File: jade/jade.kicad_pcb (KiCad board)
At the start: 2 copper layers, 275.5 x 114.5 mm, 187 parts, among them J1 MJ-4PP-9, J2 OLED, J3 MJ-4PP-9, J4 OLED, SW1 SW_PUSH, SW10 SW_PUSH, SW11 SW_PUSH, SW12 SW_PUSH, SW13 SW_PUSH, SW14 SW_PUSH, SW15 SW_PUSH, SW16 SW_PUSH, SW17 SW_PUSH, SW18 SW_PUSH, SW19 SW_PUSH, SW2 SW_PUSH, SW20 SW_PUSH, SW21 SW_PUSH, SW22 SW_PUSH, SW23 SW_PUSH, SW24 SW_PUSH, SW25 SW_PUSH, SW26 SW_PUSH, SW27 SW_PUSH, SW28 SW_PUSH, SW29 SW_PUSH, SW3 SW_PUSH, SW30 SW_PUSH, SW31 SW_PUSH, SW32 SW_PUSH, SW33 SW_PUSH, SW34 SW_PUSH, SW35 SW_PUSH, SW36 SW_PUSH, SW37 SW_PUSH, SW38 SW_PUSH, SW39 SW_PUSH, SW4 SW_PUSH, SW40 SW_PUSH, SW41 SW_PUSH, SW42 SW_PUSH, SW43 SW_PUSH, SW44 SW_PUSH, SW45 SW_PUSH, SW46 SW_PUSH, SW47 SW_PUSH, SW48 SW_PUSH, SW5 SW_PUSH, SW6 SW_PUSH, SW7 SW_PUSH, SW8 SW_PUSH, SW9 SW_PUSH, U1 ProMicro, U2 ProMicro

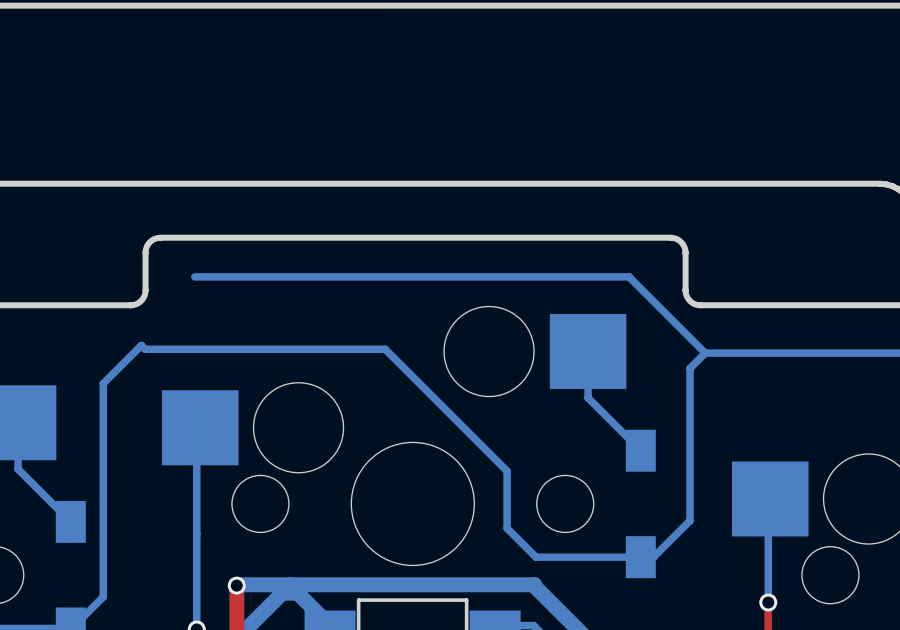
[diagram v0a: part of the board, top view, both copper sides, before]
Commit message: changed name again (cornetrack -> jade)
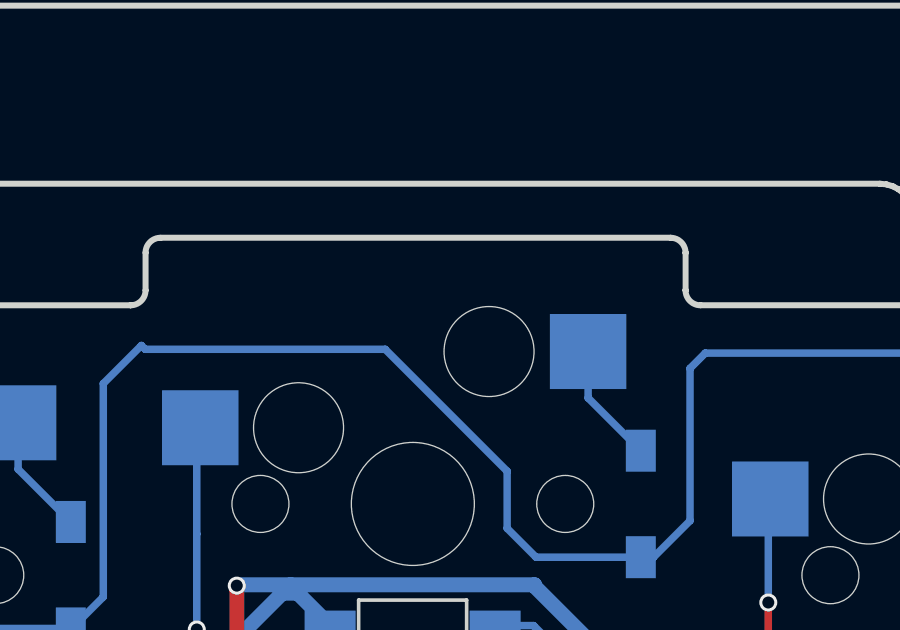
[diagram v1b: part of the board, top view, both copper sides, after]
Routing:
- net row0_r: track 205.9 -> 187.8 mm

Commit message: added breakout tabs and made pcb mostly rectangular
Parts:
- added REF**: Breakaway_Tabs, kbd:Breakaway_Tabs, B.Cu at (264.7, 102.4)
- added REF**: Breakaway_Tabs, kbd:Breakaway_Tabs, B.Cu at (223.8, 97.3)
- added REF**: Breakaway_Tabs, kbd:Breakaway_Tabs, F.Cu at (72.9, 97.3)
- added REF**: Breakaway_Tabs, kbd:Breakaway_Tabs, F.Cu at (32.0, 102.4)
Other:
- outline, holes or cut-outs redrawn

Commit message: added "break away" text to break away thingies
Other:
- board text added: "^ break away ^"

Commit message: update things
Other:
- board text added: "https://github.com/JaninaWibker"
- board text added: "https://github.com/JaninaWibker based on crkbd"
- board text added: "jdkbd pcb - designed by janina"
- board text removed: "https://github.com/JannikWibker"
- board text removed: "https://github.com/JannikWibker based on crkbd"
- board text removed: "jdkbd pcb - designed by jannikwibker"
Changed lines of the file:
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@@
     (date 2020-09-10)
     (rev 1.1)
-    (company jannikwibker)
+    (company janina)
     (comment 1 "based on crkbd / corne by foostan")
   )
@@
   (gr_circle (center 31.75 94.742) (end 32.326 94.742) (layer Edge.Cuts) (width 0.2))
   (gr_circle (center 30.988 29.972) (end 31.564 29.972) (layer Edge.Cuts) (width 0.2))
-  (gr_text "https://github.com/JannikWibker\nbased on crkbd" (at 135.128 49.276 270) (layer B.SilkS)
+  (gr_text "https://github.com/JaninaWibker\nbased on crkbd" (at 135.128 49.276 270) (layer B.SilkS)
     (effects (font (size 1 1) (thickness 0.15)) (justify mirror))
   )
-  (gr_text https://github.com/JannikWibker (at 148.082 92.202) (layer F.SilkS)
+  (gr_text https://github.com/JaninaWibker (at 148.082 92.202) (layer F.SilkS)
     (effects (font (size 1 1) (thickness 0.15)))
   )
-  (gr_text "https://github.com/JannikWibker\nbased on crkbd" (at 164.846 48.768 90) (layer B.SilkS)
+  (gr_text "https://github.com/JaninaWibker\nbased on crkbd" (at 164.846 48.768 90) (layer B.SilkS)
     (effects (font (size 1 1) (thickness 0.15)) (justify mirror))
   )
@@
   (gr_line (start 119.634 109.982) (end 126.746 97.79) (layer Edge.Cuts) (width 0.2))
   (gr_line (start 130.81 94.488) (end 133.858 94.488) (layer Edge.Cuts) (width 0.2))
-  (gr_text "jdkbd pcb - designed by jannikwibker" (at 58.166 58.166) (layer F.SilkS)
+  (gr_text "jdkbd pcb - designed by janina" (at 58.166 58.166) (layer F.SilkS)
     (effects (font (size 1 1) (thickness 0.125)) (justify left))
   )
@@
   (gr_line (start 197.9835 18.3066) (end 197.8115 18.1663) (layer Edge.Cuts) (width 0.2))
   (gr_line (start 197.8115 18.1663) (end 197.6155 18.0621) (layer Edge.Cuts) (width 0.2))
-  (gr_text "jdkbd pcb - designed by jannikwibker" (at 211.8325 58.33) (layer F.SilkS)
+  (gr_text "jdkbd pcb - designed by janina" (at 211.8325 58.33) (layer F.SilkS)
     (effects (font (size 1 1) (thickness 0.125)) (justify left))
   )
